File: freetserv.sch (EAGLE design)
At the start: 43 parts, among them IC2 SN75240PW, Q1 12MHz, Q2 6MHz, U1 MCP16311-E/MS, U4 TLV810SDBZT, U5 SN74LVC1G86DCKR

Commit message: layouted power-related part, added more MAX3232 drivers to schematics
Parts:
- added C1, C22, C23, C24, C25, C26, C27, C28, C29, C30, C31, C32, C33, C34, C35: 0.1uF, resistor:C-EUC0805
- added DRIVER0B, DRIVER0B1, DRIVER0B2: MAX3232CPWR, Texas Instruments_By_element14_Batch_1:MAX3232CPWR
- added SL2, SL3, SL4, SV2, SV3, SV4: (no value), con-lstb:MA05-1
- L3: device Wurth_Elektronik_Passive_rev15d:WE-KI_0805A -> inductor-taiyoyuden:NR6028T220M
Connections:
- new net N$11: C1.2, DRIVER0B.C1+
- new net N$20: C1.1, DRIVER0B.C1-
- new net N$21: C22.2, DRIVER0B.C2+
- new net N$22: C22.1, DRIVER0B.C2-
- new net N$23: DRIVER0B.DIN1, SERIAL0B.DB0/TXD, SV2.1
- new net N$24: DRIVER0B.ROUT1, SERIAL0B.DB1/RXD, SV2.2
- new net N$25: DRIVER0B.DOUT1, SL2.1
- new net N$26: C23.2, DRIVER0B.V+
- new net N$38: C24.2, DRIVER0B.V-
- new net N$41: DRIVER0B.RIN1, SL2.2
- new net N$47: DRIVER0B.DIN2, SERIAL0B.DB2/RTS, SV2.3
- new net N$48: DRIVER0B.ROUT2, SERIAL0B.DB3/CTS, SV2.4
- new net N$49: DRIVER0B.DOUT2, SL2.3
- new net N$50: DRIVER0B.RIN2, SL2.4
- new net N$51: C26.2, DRIVER0B1.C1+
- new net N$52: C26.1, DRIVER0B1.C1-
- new net N$53: C27.2, DRIVER0B1.C2+
- new net N$54: C27.1, DRIVER0B1.C2-
- new net N$55: DRIVER0B1.DIN1, SERIAL0C.DB0/TXD, SV3.1
- new net N$56: DRIVER0B1.ROUT1, SERIAL0C.DB1/RXD, SV3.2
- new net N$57: DRIVER0B1.DOUT1, SL3.1
- new net N$58: C28.2, DRIVER0B1.V+
- new net N$59: C29.2, DRIVER0B1.V-
- new net N$60: DRIVER0B1.RIN1, SL3.2
- new net N$61: DRIVER0B1.DIN2, SERIAL0C.DB2/RTS, SV3.3
- new net N$62: DRIVER0B1.ROUT2, SERIAL0C.DB3/CTS, SV3.4
- new net N$63: DRIVER0B1.DOUT2, SL3.3
- new net N$64: DRIVER0B1.RIN2, SL3.4
- new net N$65: C31.2, DRIVER0B2.C1+
- new net N$66: C31.1, DRIVER0B2.C1-
- new net N$67: C32.2, DRIVER0B2.C2+
- new net N$68: C32.1, DRIVER0B2.C2-
- new net N$69: DRIVER0B2.DIN1, SV4.1
- new net N$70: DRIVER0B2.ROUT1, SERIAL0D.DB1/RXD, SV4.2
- new net N$71: DRIVER0B2.DOUT1, SL4.1
- new net N$72: C33.2, DRIVER0B2.V+
- new net N$73: C34.2, DRIVER0B2.V-
- new net N$74: DRIVER0B2.RIN1, SL4.2
- new net N$75: DRIVER0B2.DIN2, SERIAL0D.DB2/RTS, SV4.3
- new net N$76: DRIVER0B2.ROUT2, SERIAL0D.DB3/CTS, SV4.4
- new net N$77: DRIVER0B2.DOUT2, SL4.3
- new net N$78: DRIVER0B2.RIN2, SL4.4
- net GND: now also C23.1, C24.1, C25.1, C28.1, C29.1, C30.1, C33.1, C34.1, C35.1, DRIVER0B.GND, DRIVER0B1.GND, DRIVER0B2.GND, SL2.5, SL3.5, SL4.5, SV2.5, SV3.5, SV4.5
- net VCC_3.3V: now also C25.2, C30.2, C35.2, DRIVER0B.VCC, DRIVER0B1.VCC, DRIVER0B2.VCC

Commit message: layout all MAX3232s, position power distribution
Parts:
- removed SL2, SL3, SL4, SV2, SV3, SV4: (no value), con-lstb:MA05-1
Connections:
- removed net N$25: DRIVER0B.DOUT1, SL2.1
- removed net N$41: DRIVER0B.RIN1, SL2.2
- removed net N$49: DRIVER0B.DOUT2, SL2.3
- removed net N$50: DRIVER0B.RIN2, SL2.4
- removed net N$57: DRIVER0B1.DOUT1, SL3.1
- removed net N$60: DRIVER0B1.RIN1, SL3.2
- removed net N$63: DRIVER0B1.DOUT2, SL3.3
- removed net N$64: DRIVER0B1.RIN2, SL3.4
- removed net N$71: DRIVER0B2.DOUT1, SL4.1
- removed net N$74: DRIVER0B2.RIN1, SL4.2
- removed net N$77: DRIVER0B2.DOUT2, SL4.3
- removed net N$78: DRIVER0B2.RIN2, SL4.4
- net GND: no longer SL2.5, SL3.5, SL4.5, SV2.5, SV3.5, SV4.5
- net N$23: no longer SV2.1
- net N$24: no longer SV2.2
- net N$47: no longer SV2.3
- net N$48: no longer SV2.4
- net N$55: no longer SV3.1
- net N$56: no longer SV3.2
- net N$61: no longer SV3.3
- net N$62: no longer SV3.4
- net N$69: no longer SV4.1
- net N$70: no longer SV4.2
- net N$75: no longer SV4.3
- net N$76: no longer SV4.4

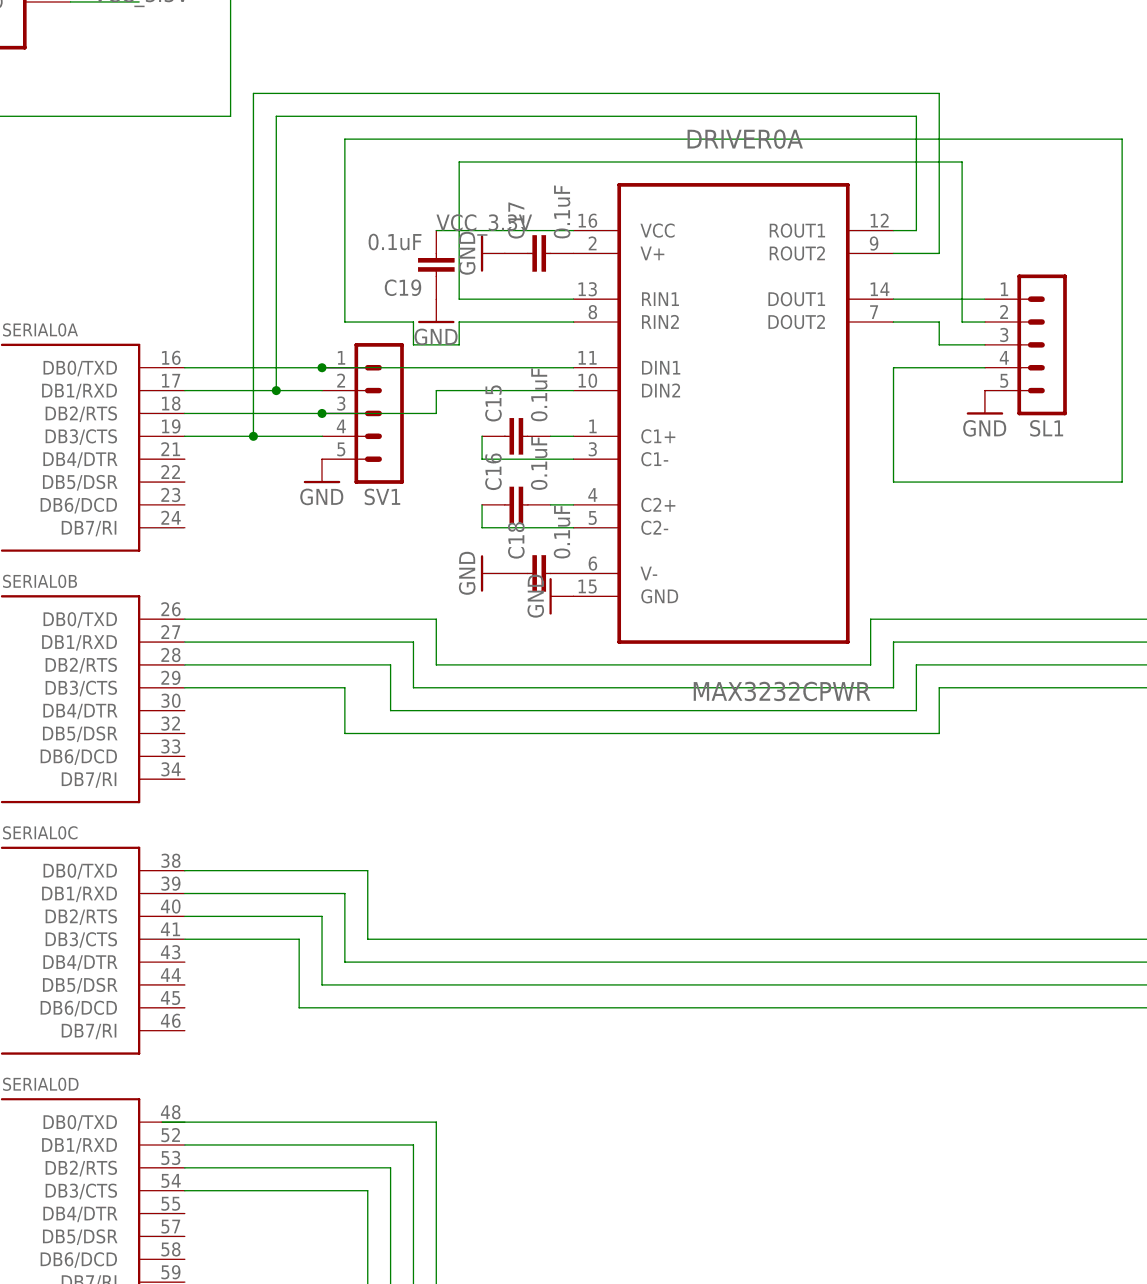
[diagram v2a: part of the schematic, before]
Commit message: routed the MAX3232 and FT4232HL within final space constraints
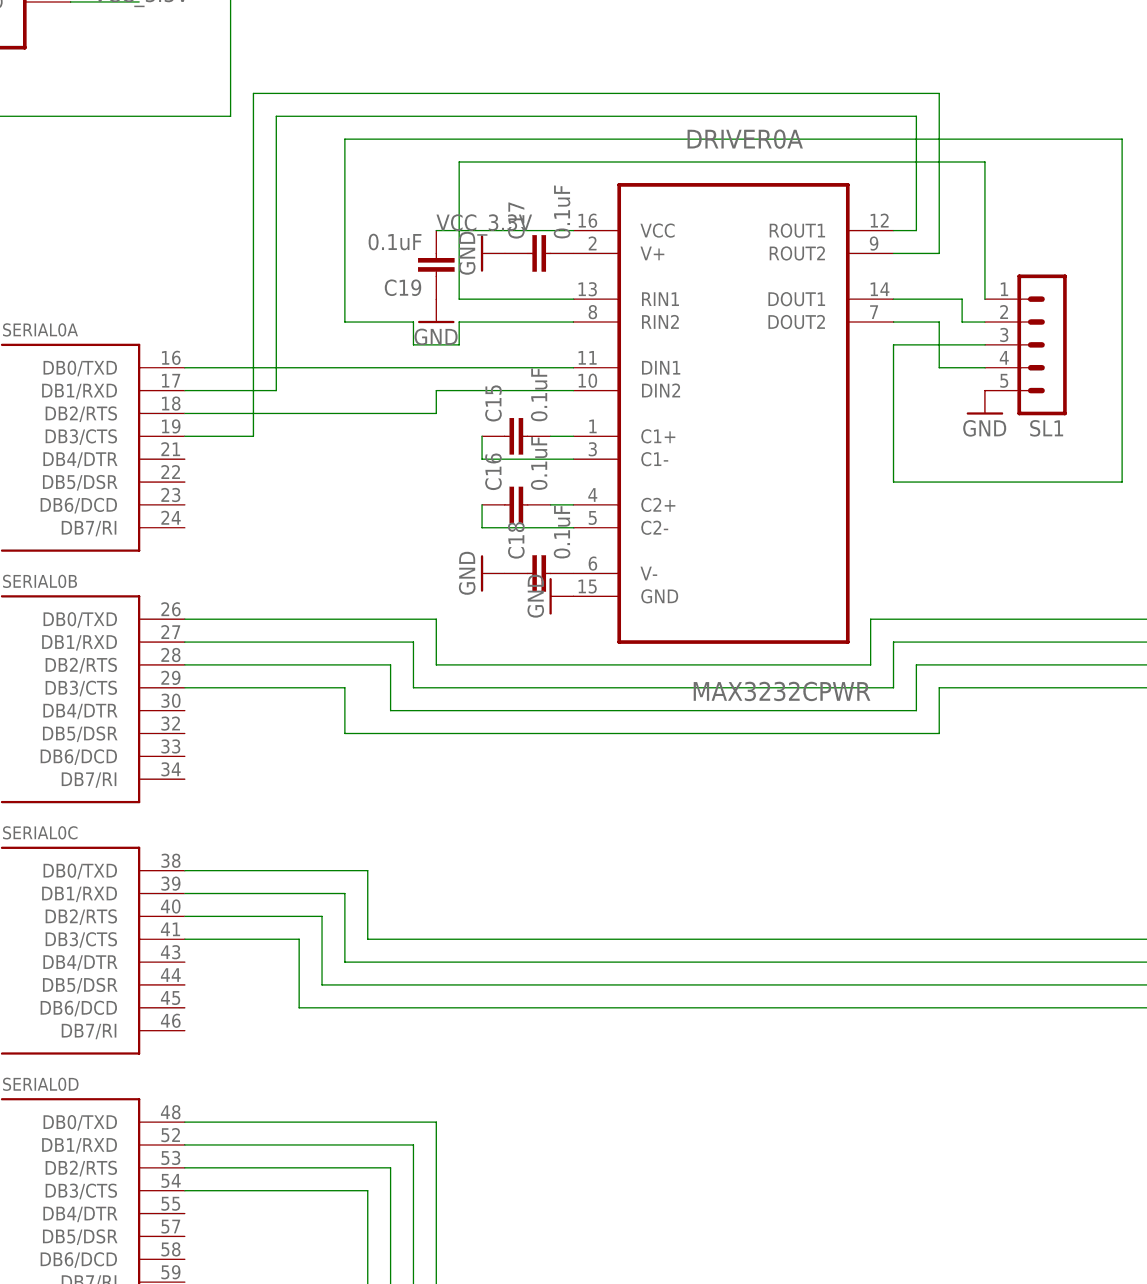
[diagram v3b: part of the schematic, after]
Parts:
- removed SV1: (no value), con-lstb:MA05-1
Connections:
- removed net N$37: DRIVER0A.DOUT1, SL1.1
- new net N$25: DRIVER0A.DOUT1, SL1.2
- net GND: no longer SV1.5
- net N$19: now also SL1.1; no longer SL1.2
- net N$35: no longer SV1.1
- net N$36: no longer SV1.2
- net N$5: no longer SV1.3
- net N$69: now also SERIAL0D.DB0/TXD
- net N$7: no longer SV1.4
- net N$8: now also SL1.4; no longer SL1.3
- net N$9: now also SL1.3; no longer SL1.4
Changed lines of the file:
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@@
 <part name="GND23" library="supply1" deviceset="GND" device=""/>
 <part name="GND24" library="supply1" deviceset="GND" device=""/>
-<part name="SV1" library="con-lstb" deviceset="MA05-1" device=""/>
 <part name="U4" library="Texas Instruments_By_element14_Batch_1" deviceset="TLV810SDBZT" device=""/>
 <part name="DRIVER0A" library="Texas Instruments_By_element14_Batch_1" deviceset="MAX3232CPWR" device=""/>
@@
 <part name="C6" library="resistor" deviceset="C-EU" device="C0805" value="10uF"/>
 <part name="C7" library="resistor" deviceset="C-EU" device="C0805" value="10uF"/>
-<part name="GND9" library="supply1" deviceset="GND" device=""/>
 <part name="GND11" library="supply1" deviceset="GND" device=""/>
 <part name="DRIVER0B" library="Texas Instruments_By_element14_Batch_1" deviceset="MAX3232CPWR" device=""/>
@@
 <instance part="GND23" gate="1" x="45.72" y="109.22" rot="R90"/>
 <instance part="GND24" gate="1" x="45.72" y="99.06" rot="R90"/>
-<instance part="SV1" gate="G$1" x="121.92" y="96.52" rot="R180"/>
 <instance part="U4" gate="A" x="-91.44" y="185.42"/>
 <instance part="DRIVER0A" gate="A" x="160.02" y="99.06"/>
@@
 <instance part="C6" gate="G$1" x="-63.5" y="228.6"/>
 <instance part="C7" gate="G$1" x="-53.34" y="228.6"/>
-<instance part="GND9" gate="1" x="114.3" y="88.9"/>
 <instance part="GND11" gate="1" x="187.96" y="96.52"/>
 <instance part="DRIVER0B" gate="A" x="269.24" y="71.12"/>
@@
 </segment>
 <segment>
-<pinref part="SV1" gate="G$1" pin="5"/>
-<pinref part="GND9" gate="1" pin="GND"/>
-</segment>
-<segment>
 <pinref part="SL1" gate="G$1" pin="5"/>
 <pinref part="GND11" gate="1" pin="GND"/>
@@
 <segment>
 <pinref part="DRIVER0A" gate="A" pin="DIN1"/>
-<wire x1="142.24" y1="101.6" x2="114.3" y2="101.6" width="0.1524" layer="91"/>
+<wire x1="142.24" y1="101.6" x2="99.06" y2="101.6" width="0.1524" layer="91"/>
 <pinref part="SERIAL0" gate="A" pin="DB0/TXD"/>
-<pinref part="SV1" gate="G$1" pin="1"/>
-<wire x1="114.3" y1="101.6" x2="99.06" y2="101.6" width="0.1524" layer="91"/>
-<junction x="114.3" y="101.6"/>
 </segment>
 </net>
@@
 <wire x1="109.22" y1="129.54" x2="109.22" y2="99.06" width="0.1524" layer="91"/>
 <pinref part="SERIAL0" gate="A" pin="DB1/RXD"/>
-<pinref part="SV1" gate="G$1" pin="2"/>
-<wire x1="114.3" y1="99.06" x2="109.22" y2="99.06" width="0.1524" layer="91"/>
-<junction x="109.22" y="99.06"/>
 <wire x1="109.22" y1="99.06" x2="99.06" y2="99.06" width="0.1524" layer="91"/>
-</segment>
-</net>
-<net name="N$37" class="0">
-<segment>
-<pinref part="DRIVER0A" gate="A" pin="DOUT1"/>
-<pinref part="SL1" gate="G$1" pin="1"/>
-<wire x1="177.8" y1="109.22" x2="187.96" y2="109.22" width="0.1524" layer="91"/>
 </segment>
 </net>
@@
 <wire x1="142.24" y1="109.22" x2="129.54" y2="109.22" width="0.1524" layer="91"/>
 <wire x1="129.54" y1="109.22" x2="129.54" y2="124.46" width="0.1524" layer="91"/>
-<wire x1="129.54" y1="124.46" x2="185.42" y2="124.46" width="0.1524" layer="91"/>
-<pinref part="SL1" gate="G$1" pin="2"/>
-<wire x1="187.96" y1="106.68" x2="185.42" y2="106.68" width="0.1524" layer="91"/>
-<wire x1="185.42" y1="106.68" x2="185.42" y2="124.46" width="0.1524" layer="91"/>
+<wire x1="129.54" y1="124.46" x2="187.96" y2="124.46" width="0.1524" layer="91"/>
+<pinref part="SL1" gate="G$1" pin="1"/>
+<wire x1="187.96" y1="124.46" x2="187.96" y2="109.22" width="0.1524" layer="91"/>
 </segment>
 </net>
@@
 <segment>
 <pinref part="SERIAL0" gate="A" pin="DB2/RTS"/>
-<pinref part="SV1" gate="G$1" pin="3"/>
-<wire x1="99.06" y1="96.52" x2="114.3" y2="96.52" width="0.1524" layer="91"/>
-<wire x1="114.3" y1="96.52" x2="127" y2="96.52" width="0.1524" layer="91"/>
+<wire x1="99.06" y1="96.52" x2="127" y2="96.52" width="0.1524" layer="91"/>
 <wire x1="127" y1="96.52" x2="127" y2="99.06" width="0.1524" layer="91"/>
 <pinref part="DRIVER0A" gate="A" pin="DIN2"/>
 <wire x1="127" y1="99.06" x2="142.24" y2="99.06" width="0.1524" layer="91"/>
-<junction x="114.3" y="96.52"/>
 </segment>
 </net>
@@
 <segment>
 <pinref part="SERIAL0" gate="A" pin="DB3/CTS"/>
-<pinref part="SV1" gate="G$1" pin="4"/>
 <wire x1="99.06" y1="93.98" x2="106.68" y2="93.98" width="0.1524" layer="91"/>
 <pinref part="DRIVER0A" gate="A" pin="ROUT2"/>
-<wire x1="106.68" y1="93.98" x2="114.3" y2="93.98" width="0.1524" layer="91"/>
 <wire x1="177.8" y1="114.3" x2="182.88" y2="114.3" width="0.1524" layer="91"/>
 <wire x1="182.88" y1="114.3" x2="182.88" y2="132.08" width="0.1524" layer="91"/>
 <wire x1="182.88" y1="132.08" x2="106.68" y2="132.08" width="0.1524" layer="91"/>
 <wire x1="106.68" y1="132.08" x2="106.68" y2="93.98" width="0.1524" layer="91"/>
-<junction x="106.68" y="93.98"/>
 </segment>
 </net>
@@
 <pinref part="DRIVER0A" gate="A" pin="DOUT2"/>
 <wire x1="177.8" y1="106.68" x2="182.88" y2="106.68" width="0.1524" layer="91"/>
-<wire x1="182.88" y1="106.68" x2="182.88" y2="104.14" width="0.1524" layer="91"/>
-<pinref part="SL1" gate="G$1" pin="3"/>
-<wire x1="182.88" y1="104.14" x2="187.96" y2="104.14" width="0.1524" layer="91"/>
+<wire x1="182.88" y1="106.68" x2="182.88" y2="101.6" width="0.1524" layer="91"/>
+<pinref part="SL1" gate="G$1" pin="4"/>
+<wire x1="182.88" y1="101.6" x2="187.96" y2="101.6" width="0.1524" layer="91"/>
 </segment>
 </net>
@@
 <wire x1="203.2" y1="127" x2="203.2" y2="88.9" width="0.1524" layer="91"/>
 <wire x1="203.2" y1="88.9" x2="177.8" y2="88.9" width="0.1524" layer="91"/>
-<wire x1="177.8" y1="88.9" x2="177.8" y2="101.6" width="0.1524" layer="91"/>
-<pinref part="SL1" gate="G$1" pin="4"/>
-<wire x1="177.8" y1="101.6" x2="187.96" y2="101.6" width="0.1524" layer="91"/>
+<wire x1="177.8" y1="88.9" x2="177.8" y2="104.14" width="0.1524" layer="91"/>
+<pinref part="SL1" gate="G$1" pin="3"/>
+<wire x1="187.96" y1="104.14" x2="177.8" y2="104.14" width="0.1524" layer="91"/>
 </segment>
 </net>
@@
 <wire x1="429.26" y1="-12.7" x2="127" y2="-12.7" width="0.1524" layer="91"/>
 <wire x1="127" y1="-12.7" x2="127" y2="17.78" width="0.1524" layer="91"/>
-<wire x1="127" y1="17.78" x2="96.52" y2="17.78" width="0.1524" layer="91"/>
+<pinref part="SERIAL0" gate="D" pin="DB0/TXD"/>
+<wire x1="99.06" y1="17.78" x2="127" y2="17.78" width="0.1524" layer="91"/>
 </segment>
 </net>
@@
 </segment>
 </net>
+<net name="N$25" class="0">
+<segment>
+<pinref part="SL1" gate="G$1" pin="2"/>
+<wire x1="187.96" y1="106.68" x2="185.42" y2="106.68" width="0.1524" layer="91"/>
+<wire x1="185.42" y1="106.68" x2="185.42" y2="109.22" width="0.1524" layer="91"/>
+<pinref part="DRIVER0A" gate="A" pin="DOUT1"/>
+<wire x1="185.42" y1="109.22" x2="177.8" y2="109.22" width="0.1524" layer="91"/>
+</segment>
+</net>
